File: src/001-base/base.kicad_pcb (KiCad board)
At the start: 2 copper layers, 99 x 99 mm, 397 parts

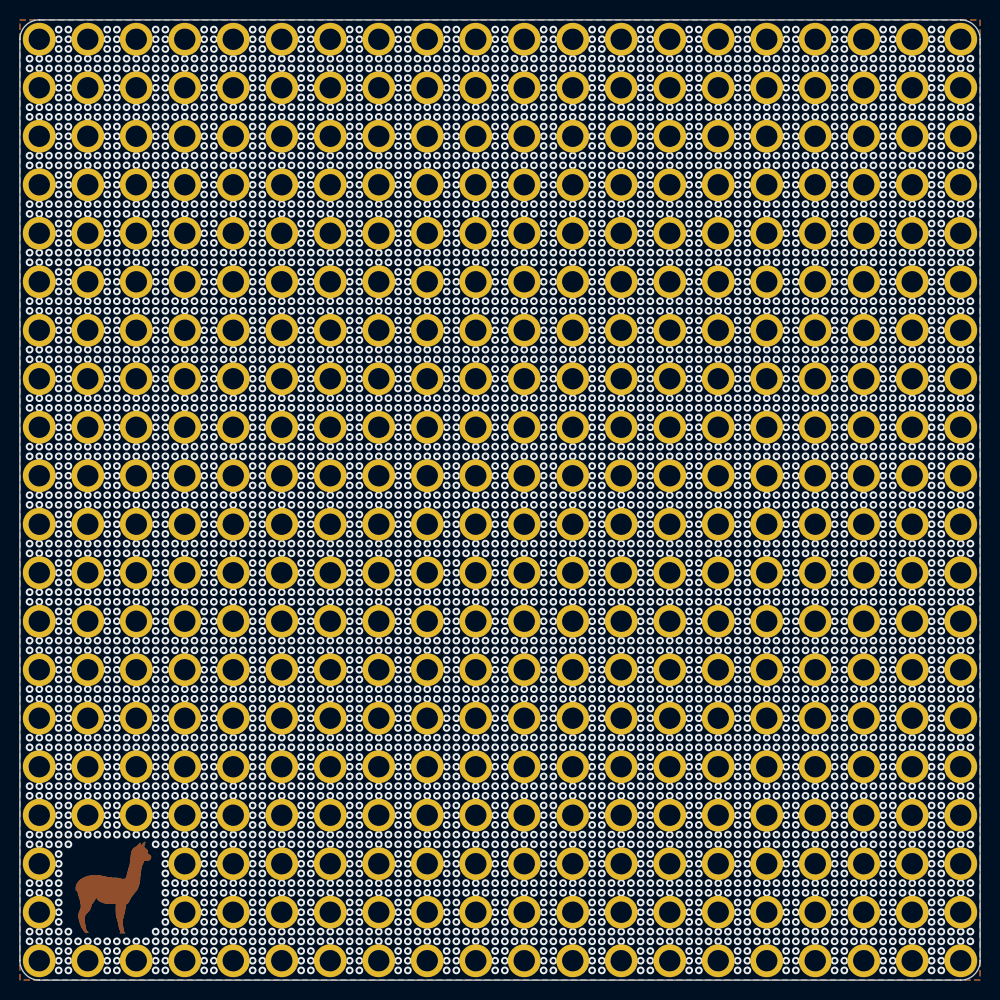
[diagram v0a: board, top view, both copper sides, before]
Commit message: Update M2 hole size in 001 base plate
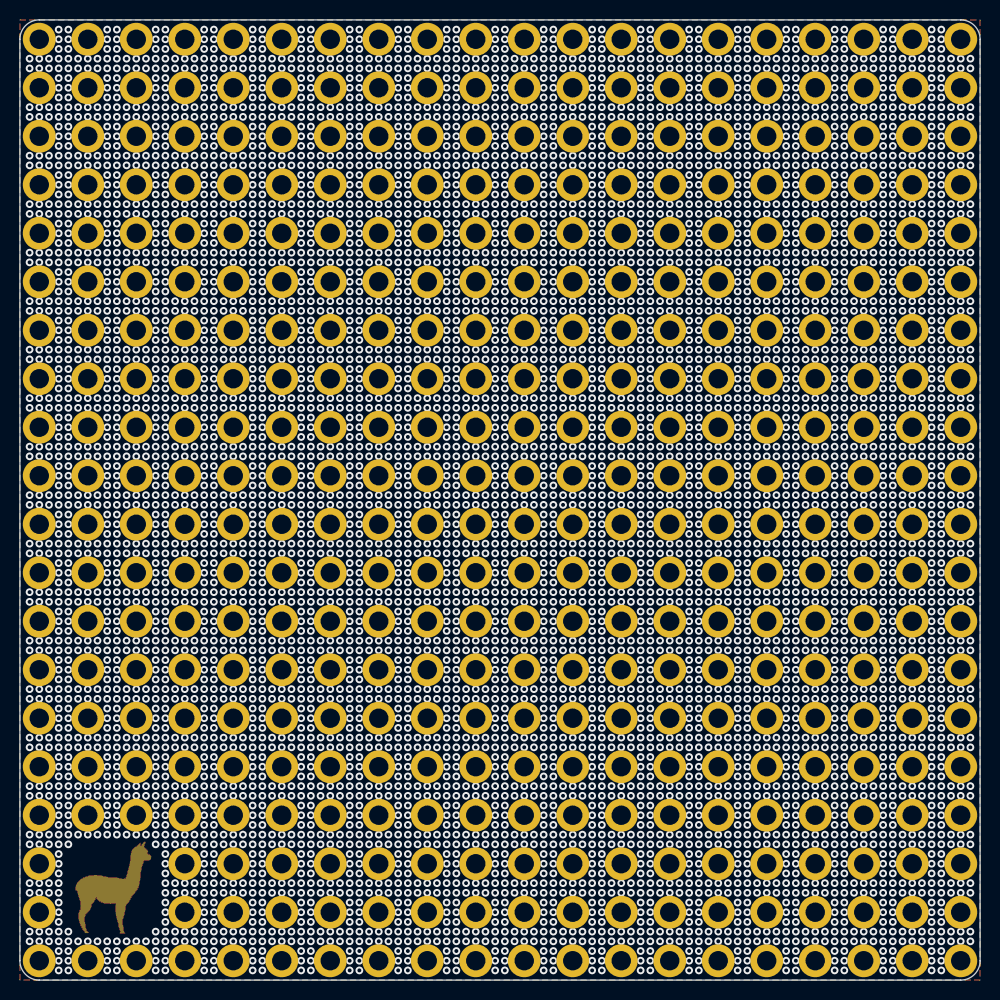
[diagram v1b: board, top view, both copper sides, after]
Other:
- board text added: "001 REV2"
- board text removed: "001"
